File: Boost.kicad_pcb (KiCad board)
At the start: 2 copper layers, 200 x 100 mm, 23 parts, among them Q1 IRFZ44N, U1 UC3843_DIP8

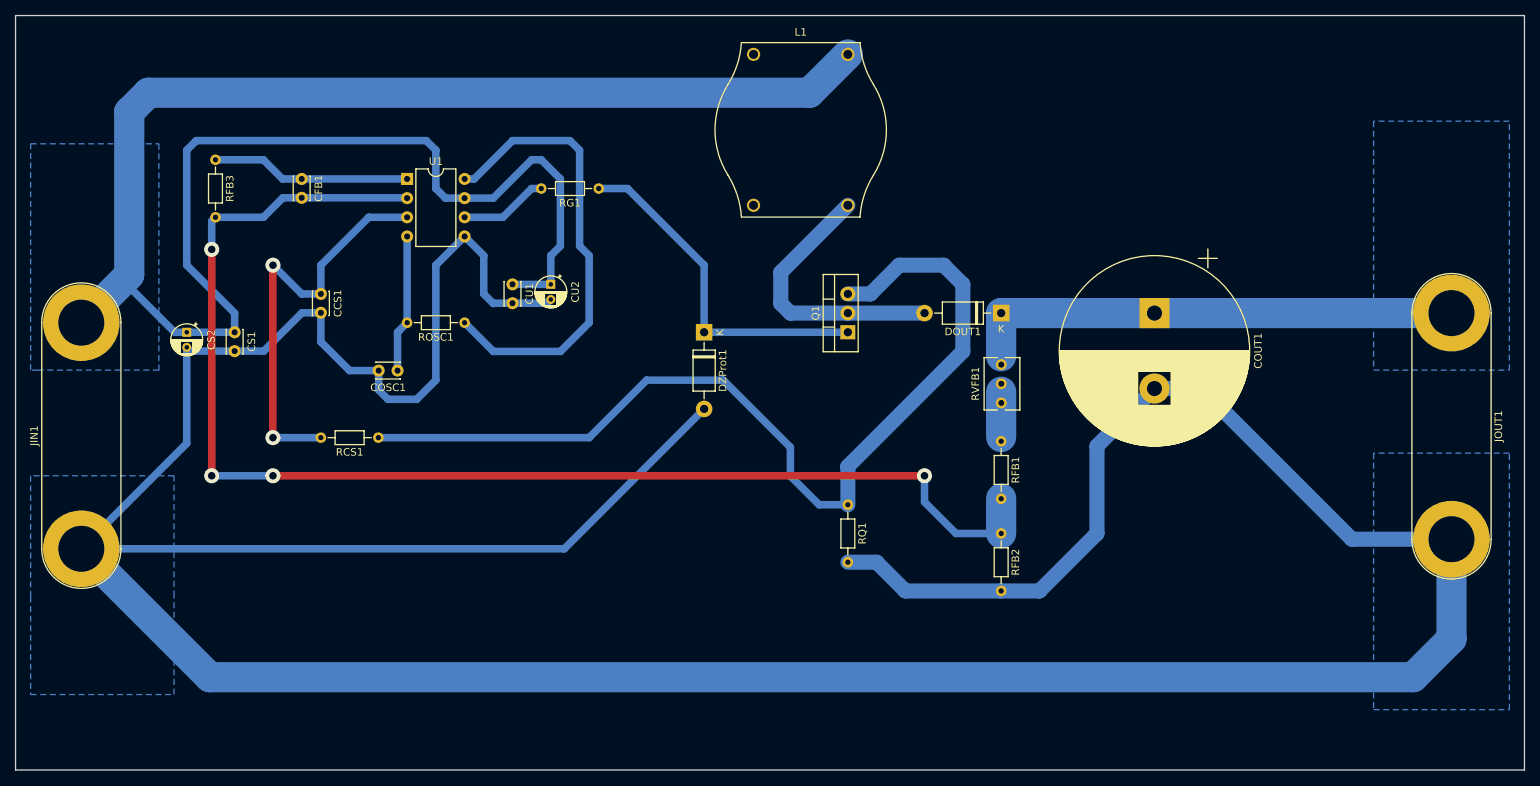
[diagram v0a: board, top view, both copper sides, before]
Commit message: Reducción de placa
Se redujo la placa de 10cm x 20cm a 5cm x 10 cm.
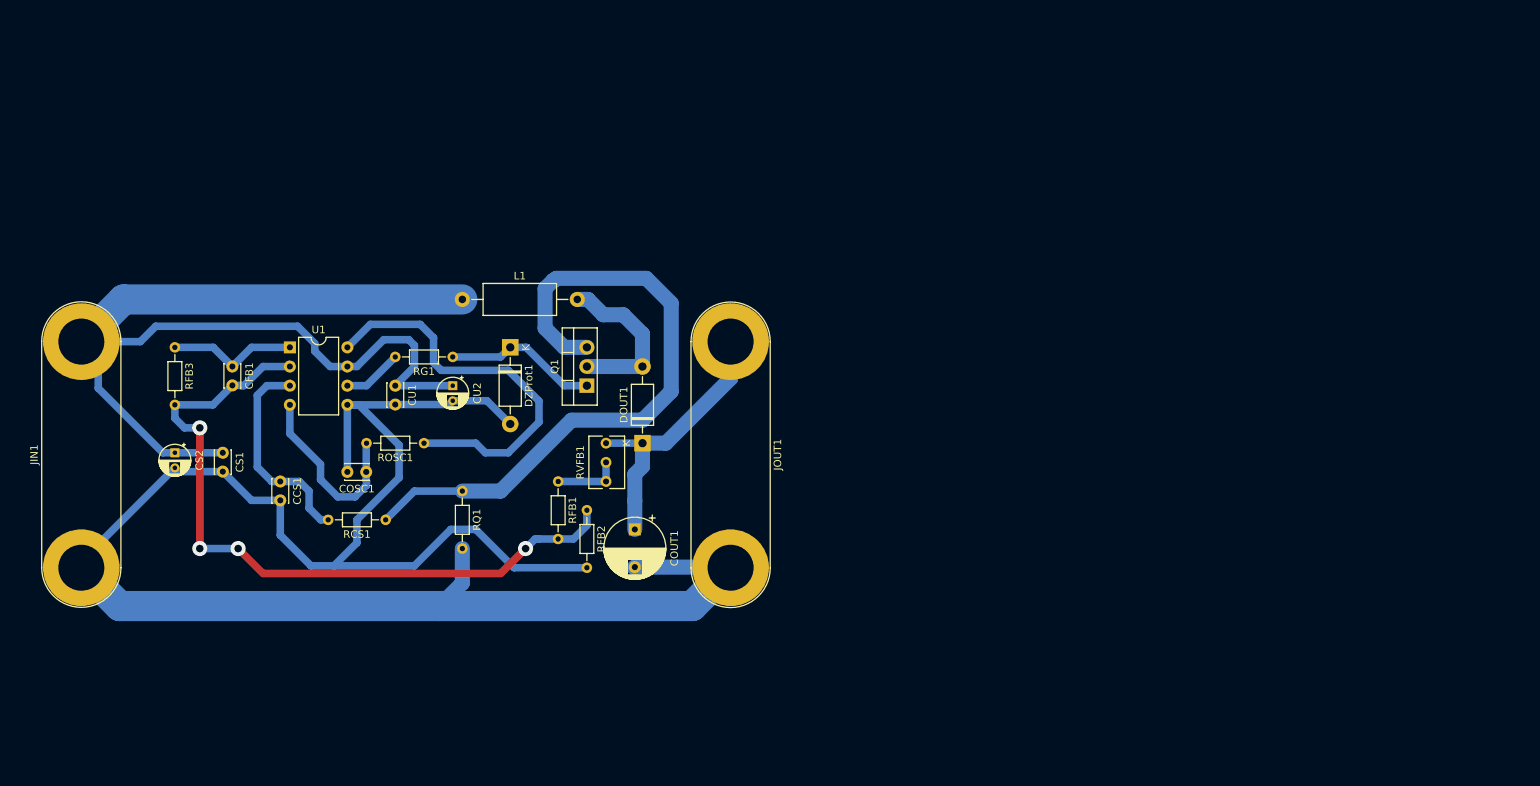
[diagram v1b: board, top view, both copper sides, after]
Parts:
- COUT1: footprint Capacitor_THT:CP_Radial_D25.0mm_P10.00mm_SnapIn -> Capacitor_THT:CP_Radial_D8.0mm_P5.00mm
- L1: footprint Inductor_THT:Choke_EPCOS_B82722A -> Inductor_THT:L_Axial_L9.5mm_D4.0mm_P15.24mm_Horizontal_Fastron_SMCC
- moved JOUT1 95.6 mm to (144.8, 93.2)
- moved COUT1 74.6 mm to (132.1, 118.1)
- moved L1 60.5 mm to (109.2, 87.6), turned to 0 degrees
- moved RFB1 59.0 mm to (121.9, 111.8)
- moved RFB2 55.0 mm to (125.7, 115.6)
- moved RVFB1 53.4 mm to (128.3, 106.7)
- moved RQ1 51.1 mm to (109.2, 113.0)
- moved DOUT1 50.6 mm to (133.1, 106.7), turned to 90 degrees
- moved Q1 35.3 mm to (125.7, 99.1)
- moved RG1 29.5 mm to (108.0, 95.2)
- moved U1 27.2 mm to (86.4, 94.0)
- moved CFB1 26.5 mm to (78.7, 96.5)
- moved DZProt1 25.8 mm to (115.6, 94.0)
- moved CCS1 25.4 mm to (85.1, 111.8)
- moved RFB3 25.4 mm to (71.1, 94.0)
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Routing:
- net Earth: track 518.3 -> 257.8 mm
- net +15V: track 252.7 -> 143.6 mm
- net Net-(CFB1-Pad2): track 175.4 -> 96.3 mm
- net Net-(Q1-Pad3): track 127.8 -> 87.1 mm
- net Net-(COUT1-Pad1): track 65.4 -> 36.8 mm
- net Net-(CCS1-Pad1): track 55.0 -> 28.0 mm, vias 2 -> 0
- net Net-(DZProt1-Pad1): track 46.1 -> 20.4 mm
- net Net-(DOUT1-Pad2): track 36.3 -> 22.2 mm
- net Net-(CFB1-Pad1): track 26.5 -> 17.3 mm
- net Net-(ROSC1-Pad1): track 60.9 -> 53.0 mm
- net Net-(COSC1-Pad1): track 18.3 -> 24.9 mm
- net Net-(RG1-Pad2): track 11.7 -> 7.93 mm
- net Net-(RFB1-Pad1): track 6.02 -> 8.89 mm
- removed copper zone on B.Cu, net +15V
- removed copper zone on B.Cu, net Earth
- removed copper zone on B.Cu, net Net-(COUT1-Pad1)
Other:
- board outline removed

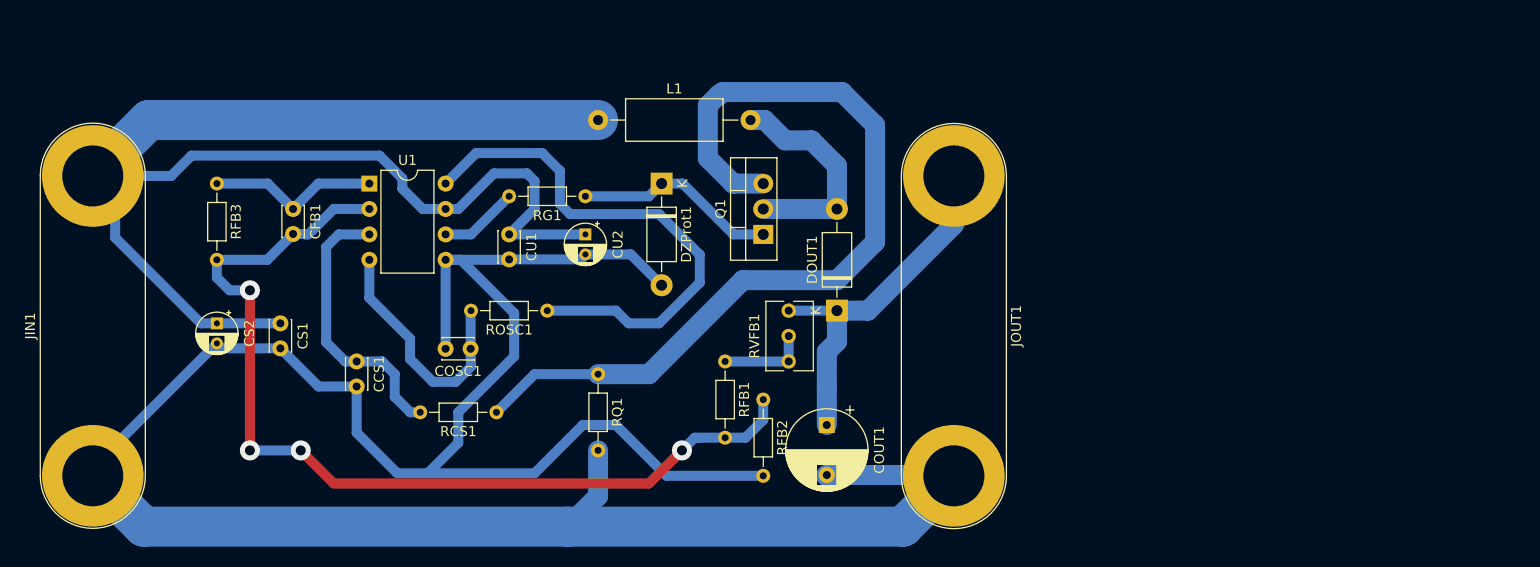
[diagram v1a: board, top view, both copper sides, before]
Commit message: Emprolijando el puente de feedback
Emprolije el puente de la realimentación, que habia quedado sobre una RQ1.
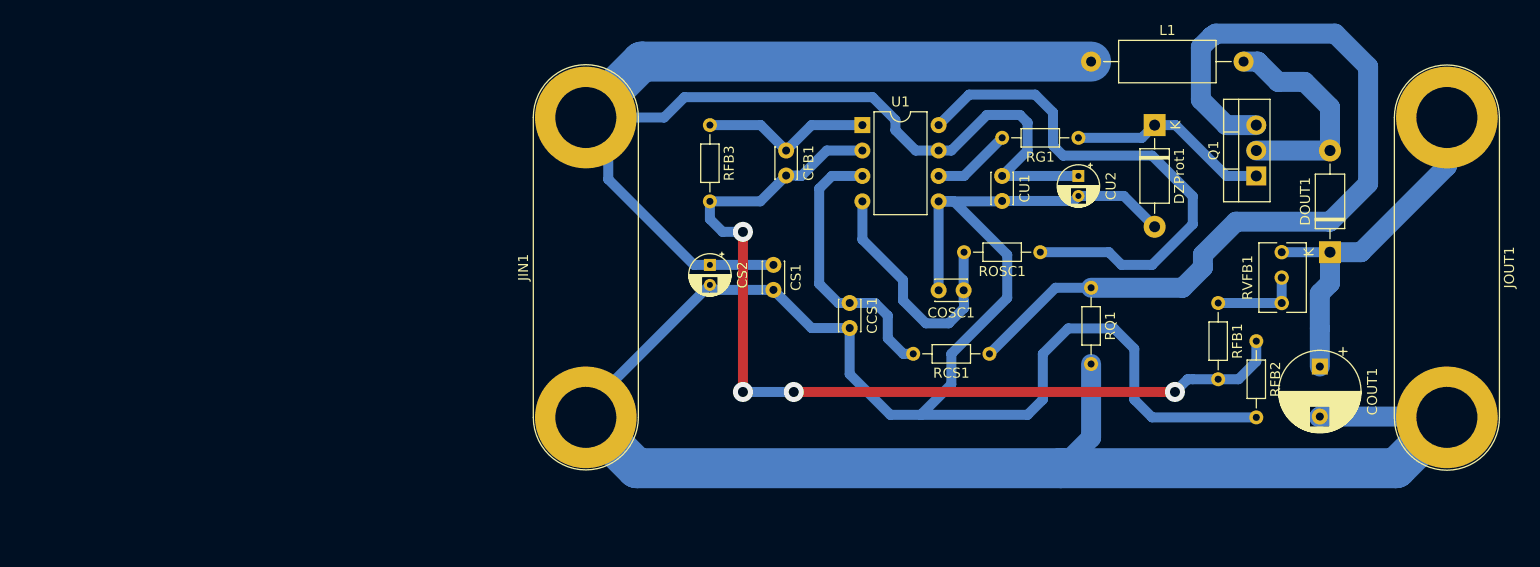
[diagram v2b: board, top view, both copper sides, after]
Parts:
- moved RQ1 50.0 mm to (158.5, 104.4)
- moved CCS1 49.6 mm to (134.4, 105.9)
- moved DOUT1 49.6 mm to (182.4, 100.8)
- moved DZProt1 49.6 mm to (164.8, 88.1)
- moved JOUT1 49.6 mm to (194.1, 87.4)
- moved L1 49.6 mm to (158.5, 81.8)
- moved RCS1 49.6 mm to (148.3, 111.0)
- moved CFB1 49.6 mm to (128.0, 90.7)
- moved COSC1 49.6 mm to (145.8, 104.6)
- moved CS1 49.6 mm to (126.7, 102.1)
- moved CS2 49.6 mm to (120.4, 102.1)
- moved CU1 49.6 mm to (149.6, 93.2)
- moved CU2 49.6 mm to (157.2, 93.2)
- moved JIN1 49.6 mm to (108.0, 117.3)
- moved Q1 49.6 mm to (175.0, 93.2)
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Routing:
- net Earth: track 257.8 -> 269.4 mm
- net Net-(CFB1-Pad2): track 96.3 -> 93.6 mm
- net Net-(Q1-Pad3): track 87.1 -> 87.8 mm
